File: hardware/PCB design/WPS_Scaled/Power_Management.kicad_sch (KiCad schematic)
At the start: 17 parts, among them J1 KF128-5.08-2P, Q1 2N2222, Q2 IRF9540NPBF, U1 LM2595T-5.0, U2 MCP1702T-3302E/MB

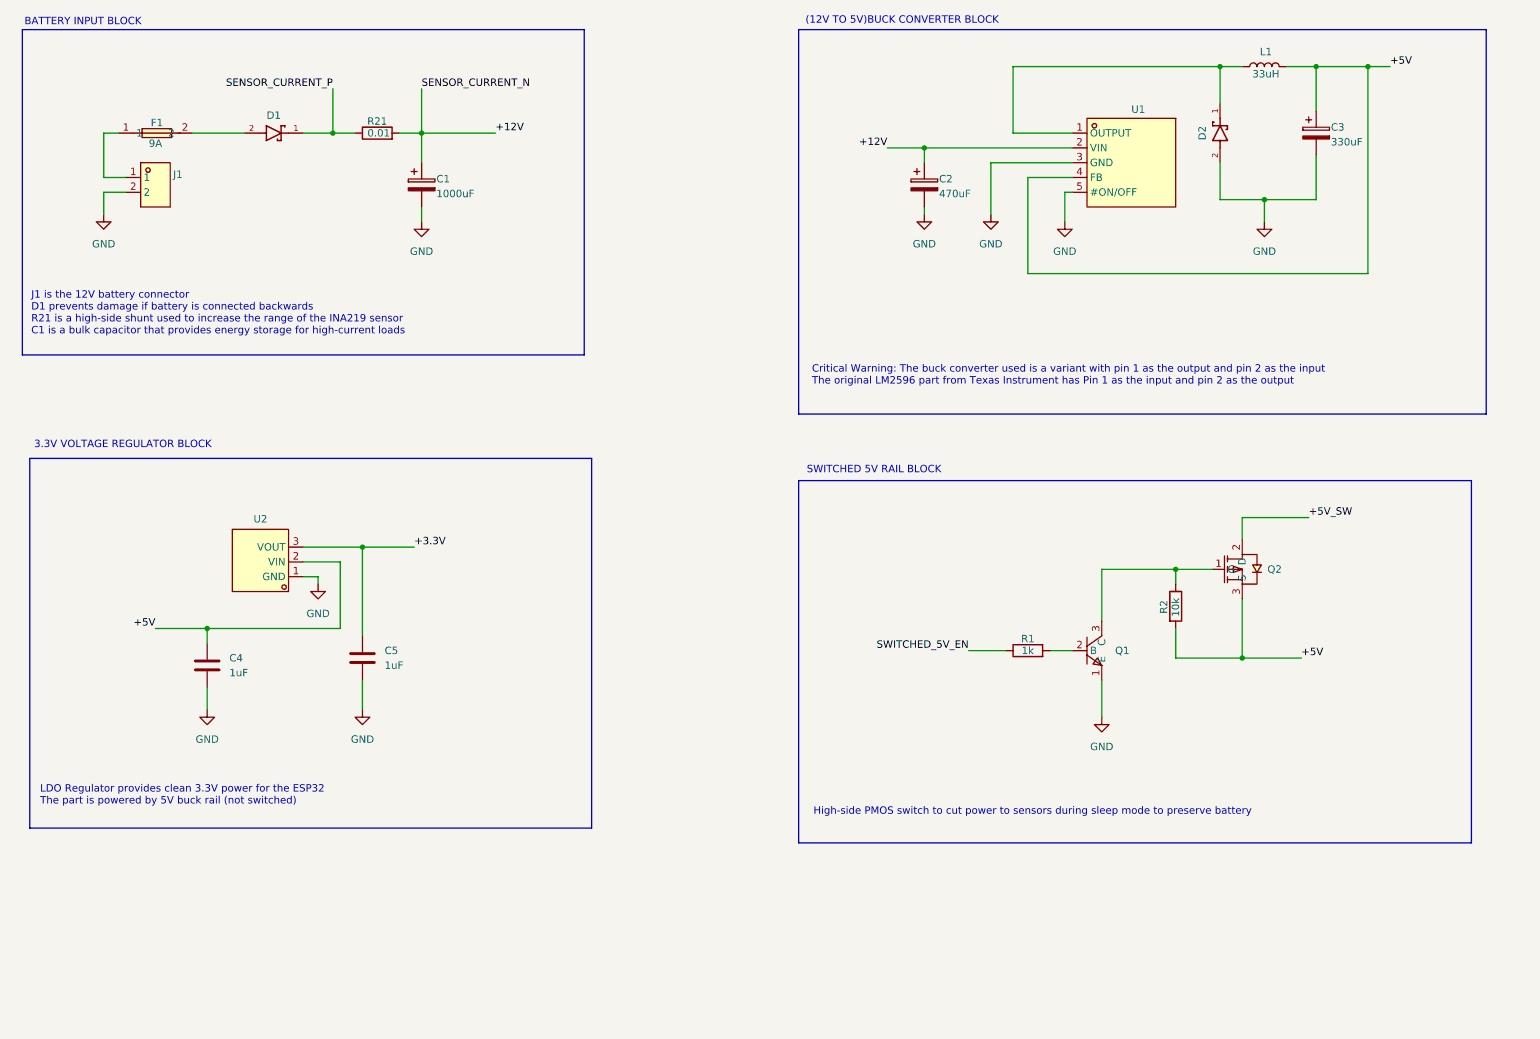
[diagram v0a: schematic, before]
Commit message: finalized with the sensors and actuator schematics
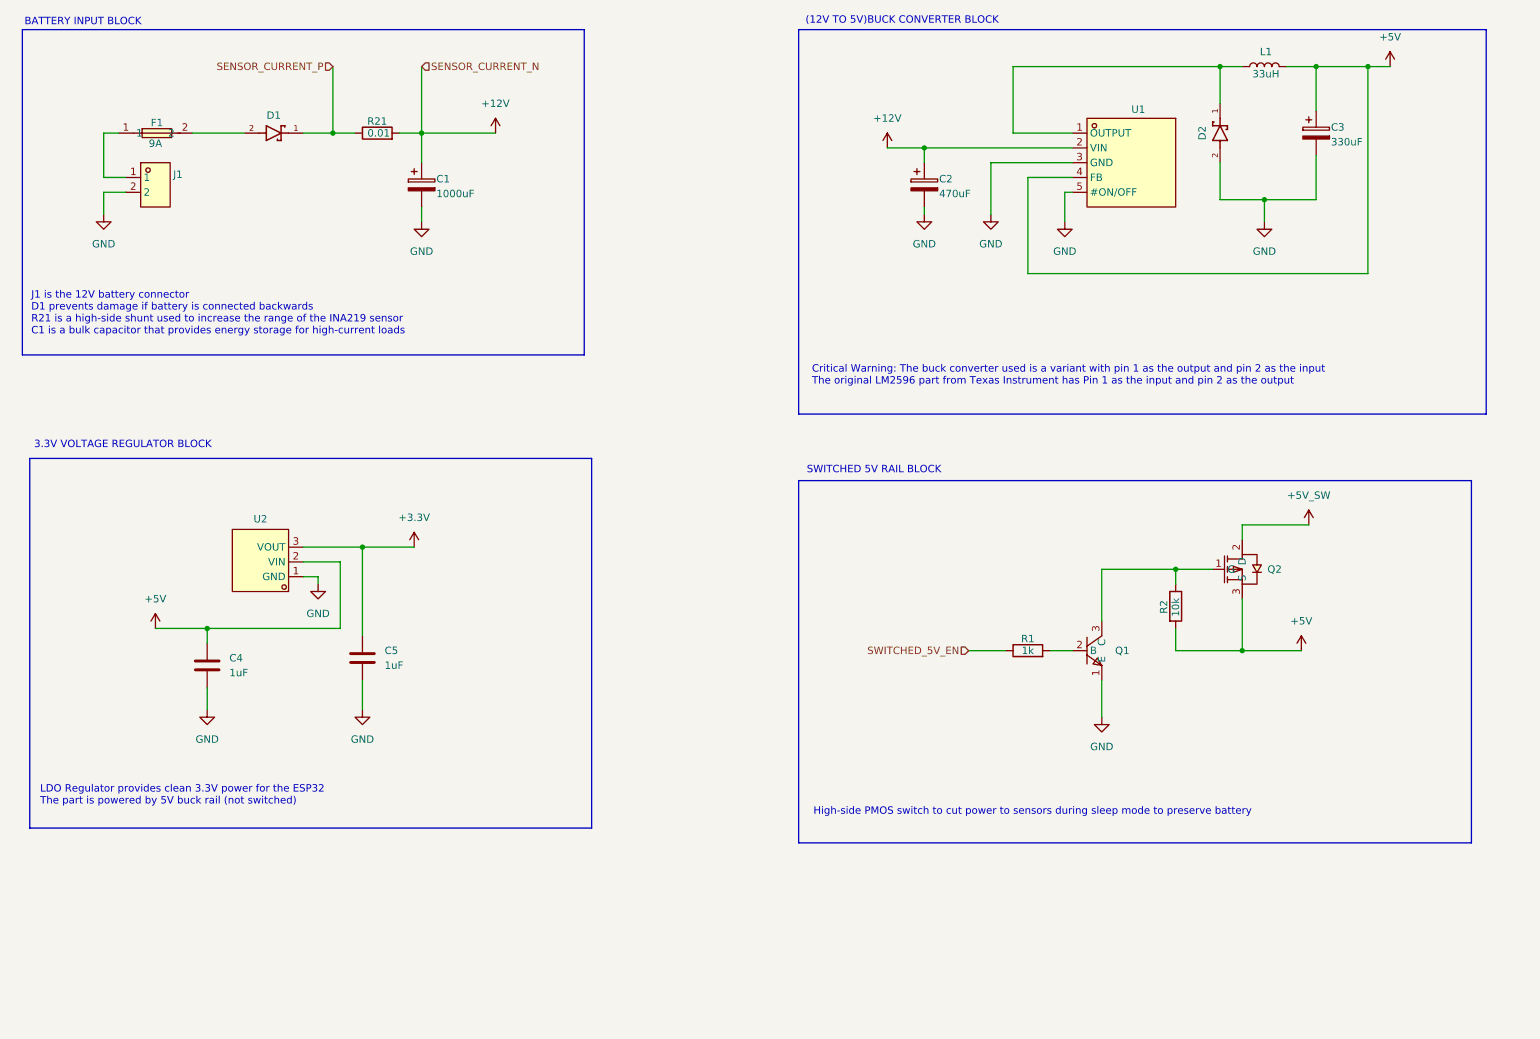
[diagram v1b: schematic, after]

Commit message: finalized the pcb schematics
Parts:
- added D11: 1N5817-T, 1N5817-T:DIOAD1039W78L463D236, symbol COIL_1N5817-T:1N5817-T
- added TP_12V1, TP_3.3V1, TP_5V1, TP_GND1: TestPoint, symbol Connector:TestPoint
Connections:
- net +12V: now also TP_12V1.1
- net +3.3V: now also TP_3.3V1.1
- net +5V: now also D11.1; no longer C3.1, L1.2, U1.4 (FB)
- net GND: now also TP_GND1.1
- new net: C3.1, D11.2, L1.2, TP_5V1.1, U1.4 (FB)
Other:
- company: (none) -> Makerere University
- moved on the sheet: C2, C3, C4, D2, L1, U1

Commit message: finallized pcb layout
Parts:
- removed TP_3.3V1: TestPoint, symbol Connector:TestPoint
- removed U2: MCP1702T-3302E/MB, :SOT-89-3_L4.5-W2.5-P1.50-LS4.2-BR, symbol COIL:MCP1702T-3302E_MB
- added NT1: NetTie_2, NetTie:NetTie-2_SMD_Pad2.0mm, symbol Device:NetTie_2
- added TP4: 3.3V, TestPoint:TestPoint_THTPad_D2.0mm_Drill1.0mm, symbol Connector:TestPoint
- added TP5: 5V_SW, TestPoint:TestPoint_THTPad_D2.0mm_Drill1.0mm, symbol Connector:TestPoint
- added U2: TLV1117LV33DCYR, COIL:SOT-223_L6.7-W3.5-P2.30-BR, symbol COIL:TLV1117LV33DCYR
- C1, C2: footprint (none) -> COIL:CAP-TH_BD10.0-P5.00-D1.0-FD
- C3: footprint (none) -> COIL:CAP-TH_BD6.3-P2.50-D0.5-FD
- C4, C5: footprint (none) -> COIL:CAP-TH_L4.4-W4.0-P5.08-D0.6
- D1, D11, D2: footprint 1N5817-T:DIOAD1039W78L463D236 -> COIL:DO-27_BD5.2-L8.9-P12.90-D1.5-RD
- F1: footprint :FUSE-TH_L15.0-W3.0-P5.08-D1.0-S1.2 -> COIL:FUSE-TH_L15.0-W3.0-P5.08-D1.0-S1.2
- J1: footprint :CONN-TH_P5.08_KF128-5.08-2P -> COIL:CONN-TH_P5.08_KF128-5.08-2P
- L1: footprint (none) -> COIL:IND-TH_L14.0-W6.5-P8.00-D0.6
- Q1: footprint :TO-92-3_L4.9-W3.7-P1.27-L -> COIL:TO-92-3_L4.9-W3.7-P1.27-L
- Q2: footprint :TO-220-3_L10.0-W4.5-P2.54-L -> COIL:TO-220-3_L10.0-W4.5-P2.54-L
- R1, R2: footprint (none) -> COIL:RES-TH_BD2.4-L6.3-P10.30-D0.6
- R21: footprint (none) -> COIL:RES-TH_L13.0-W4.0-P10.0
- TP1: renamed from TP_12V1; value TestPoint -> 12V; footprint (none) -> TestPoint:TestPoint_THTPad_D2.0mm_Drill1.0mm
- TP2: renamed from TP_GND1; value TestPoint -> GNDPWR; footprint (none) -> TestPoint:TestPoint_THTPad_D2.0mm_Drill1.0mm
- TP3: renamed from TP_5V1; value TestPoint -> 5V; footprint (none) -> TestPoint:TestPoint_THTPad_D2.0mm_Drill1.0mm
- U1: footprint :TO-220-5L_L10.2-W4.5-P1.71-L -> COIL:TO-220-5L_L10.2-W4.5-P1.71-L
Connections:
- net +5V: now also U2.3 (IN)
- net +5V_SW: now also TP5.1
- net GND: now also NT1.2, U2.1 (ADJ/GND); no longer C1.2, C2.2, J1.2, TP2.1, U1.3 (GND), U1.5 (#ON/OFF)
- net Q1_BASE: now reaches Q1.2 (B), R1.2
- net BUCK_OUT: now reaches D2.1, L1.1, U1.1 (OUTPUT)
- net BUCK_FB: now reaches C3.1, D11.2, L1.2, TP3.1, U1.4 (FB)
- net VBAT_FUSED: now reaches D1.2, F1.2
- net VBAT_IN: now reaches F1.1, J1.1
- net Q2_GATE: now reaches Q1.3 (C), Q2.1 (G), R2.1
- net +12V renamed VBAT
- net +3.3V renamed +3V3
- net +3V3: now also TP4.1, U2.2 (OUT), U2.4 (OUT)
- new net GNDPWR: C1.2, C2.2, J1.2, NT1.1, TP2.1, U1.3 (GND), U1.5 (#ON/OFF)
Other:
- note added: "GNDPWR is the "dirty" ground for the 12V actuators GND is the "clean" ground for the 3.3 and 5V components"
- note added: "GROUND connection"
- moved on the sheet: C1, F1, J1, Q1, R1, R2, R21, TP1, TP2
